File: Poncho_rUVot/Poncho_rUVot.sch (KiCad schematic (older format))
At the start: 20 parts, among them J1 Screw_Terminal_01x03, K1 G5V-1, P1 Conn_01x03, P2 Conn_01x03, P3 Conn_01x04, P4 Conn_01x03, P5 Conn_01x02, P6 Conn_01x02, P7 Conn_01x06, P8 Conn_01x04, P9 Conn_01x08, Q1 BC548, Q2 BC548

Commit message: Se elimina erro electrico en esquematico
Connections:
- net labels removed: GNDA, GNDD
- wire segments 144 -> 135
- no-connect marks 37 -> 44
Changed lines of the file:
@@
-	1    0    0    -1
-$EndComp
-$Comp
-L Poncho_rUVot-rescue:GND #PWR06
-U 1 1 57A7A207
-P 3000 3550
-F 0 "#PWR06" H 3000 3550 30  0001 C CNN
-F 1 "GND" H 3000 3480 30  0001 C CNN
-F 2 "" H 3000 3550 60  0000 C CNN
-F 3 "" H 3000 3550 60  0000 C CNN
-	1    3000 3550
 	1    0    0    -1
 $EndComp
@@
 	1    0    0    -1
 $EndComp
-$Comp
-L Poncho_rUVot-rescue:GNDD #PWR012
-U 1 1 57A7AB5F
-P 1400 6700
-F 0 "#PWR012" H 1400 6450 50  0001 C CNN
-F 1 "GNDD" H 1400 6550 50  0000 C CNN
-F 2 "" H 1400 6700 50  0000 C CNN
-F 3 "" H 1400 6700 50  0000 C CNN
-	1    1400 6700
-	1    0    0    -1
-$EndComp
-$Comp
-L Poncho_rUVot-rescue:GNDA #PWR016
-U 1 1 57A7AE2B
-P 3300 1900
-F 0 "#PWR016" H 3300 1650 50  0001 C CNN
-F 1 "GNDA" H 3300 1750 50  0000 C CNN
-F 2 "" H 3300 1900 50  0000 C CNN
-F 3 "" H 3300 1900 50  0000 C CNN
-	1    3300 1900
-	1    0    0    -1
-$EndComp
-$Comp
-L Poncho_rUVot-rescue:GNDA #PWR017
-U 1 1 57A7AE5D
-P 1350 1800
-F 0 "#PWR017" H 1350 1550 50  0001 C CNN
-F 1 "GNDA" H 1350 1650 50  0000 C CNN
-F 2 "" H 1350 1800 50  0000 C CNN
-F 3 "" H 1350 1800 50  0000 C CNN
-	1    1350 1800
-	1    0    0    -1
-$EndComp
-Wire Wire Line
-	1600 1750 1350 1750
-Wire Wire Line
-	1350 1750 1350 1800
 Wire Wire Line
 	2800 1750 2850 1750
 Wire Wire Line
-	2850 1750 2850 1850
-Wire Wire Line
 	2850 2250 2800 2250
 Wire Wire Line
 	2800 2150 2850 2150
-Connection ~ 2850 2150
 Wire Wire Line
 	2800 2050 2850 2050
-Connection ~ 2850 2050
 Wire Wire Line
 	2800 1950 2850 1950
-Connection ~ 2850 1950
 Wire Wire Line
 	2800 1850 2850 1850
-Connection ~ 2850 1850
-Wire Wire Line
-	3300 1850 3300 1900
 Wire Wire Line
 	1600 4650 1250 4650
@@
 Wire Wire Line
 	1400 4850 1400 4950
-Wire Wire Line
-	2850 2150 2850 2250
-Wire Wire Line
-	2850 2050 2850 2150
-Wire Wire Line
-	2850 1950 2850 2050
-Wire Wire Line
-	2850 1850 2850 1950
-Wire Wire Line
-	2850 1850 3300 1850
 $Comp
 L conectores-rescue:+5V-power #PWR0105
@@
 Wire Notes Line
 	750  750  750  7150
+$Comp
+L conectores-rescue:GND-power #PWR0111
+U 1 1 608EC6E9
+P 1400 6700
+F 0 "#PWR0111" H 1400 6450 50  0001 C CNN
+F 1 "GND" H 1405 6527 50  0000 C CNN
+F 2 "" H 1400 6700 50  0001 C CNN
+F 3 "" H 1400 6700 50  0001 C CNN
+	1    1400 6700
+	1    0    0    -1
+$EndComp
+$Comp
+L conectores-rescue:GND-power #PWR0112
+U 1 1 608FA01E
+P 3000 3550
+F 0 "#PWR0112" H 3000 3300 50  0001 C CNN
+F 1 "GND" H 3005 3377 50  0000 C CNN
+F 2 "" H 3000 3550 50  0001 C CNN
+F 3 "" H 3000 3550 50  0001 C CNN
+	1    3000 3550
+	1    0    0    -1
+$EndComp
+NoConn ~ 1600 1750
+NoConn ~ 2850 1750
+NoConn ~ 2850 1850
+NoConn ~ 2850 1950
+NoConn ~ 2850 2050
+NoConn ~ 2850 2150
+NoConn ~ 2850 2250
 $EndSCHEMATC

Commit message: actualizacion
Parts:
- BZ1: footprint Buzzers_Beepers:BUZZER -> Buzzer_Beeper:Buzzer_12x9.5RM7.6; symbol conectores-rescue:Buzzer-Device -> Poncho_rUVot-rescue:Buzzer-Device-conectores-rescue
- D1: footprint Diodes_THT:D_DO-35_SOD27_P2.54mm_Vertical_AnodeUp -> Diode_THT:D_DO-35_SOD27_P10.16mm_Horizontal; symbol conectores-rescue:1N4148-Diode -> Poncho_rUVot-rescue:1N4148-Diode-conectores-rescue
- D2: footprint LEDs:LED_D5.0mm -> LED_THT:LED_D5.0mm; symbol conectores-rescue:LED-Device -> Poncho_rUVot-rescue:LED-Device-conectores-rescue
- J1: symbol conectores-rescue:Screw_Terminal_01x03-Connector -> Poncho_rUVot-rescue:Screw_Terminal_01x03-Connector-conectores-rescue
- K1: footprint TerminalBlock:TerminalBlock_bornier-3_P5.08mm -> Relay_THT:Relay_SPDT_Omron_G5V-1; symbol conectores-rescue:G5V-1-Relay -> Poncho_rUVot-rescue:G5V-1-Relay-conectores-rescue
- P1, P2, P4: symbol conectores-rescue:Conn_01x03-Connector_Generic -> Poncho_rUVot-rescue:Conn_01x03-Connector_Generic-conectores-rescue
- P3, P8: symbol conectores-rescue:Conn_01x04-Connector_Generic -> Poncho_rUVot-rescue:Conn_01x04-Connector_Generic-conectores-rescue
- P5, P6: symbol conectores-rescue:Conn_01x02-Connector_Generic -> Poncho_rUVot-rescue:Conn_01x02-Connector_Generic-conectores-rescue
- P7: symbol conectores-rescue:Conn_01x06-Connector_Generic -> Poncho_rUVot-rescue:Conn_01x06-Connector_Generic-conectores-rescue
- P9: symbol conectores-rescue:Conn_01x08-Connector_Generic -> Poncho_rUVot-rescue:Conn_01x08-Connector_Generic-conectores-rescue
- Q1, Q2: symbol conectores-rescue:BC548-Transistor_BJT -> Poncho_rUVot-rescue:BC548-Transistor_BJT-conectores-rescue
- R1, R2, R4: symbol conectores-rescue:R-Device -> Poncho_rUVot-rescue:R-Device-conectores-rescue
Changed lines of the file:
@@
 	1400 4850 1400 4950
 $Comp
-L conectores-rescue:+5V-power #PWR0105
+L Poncho_rUVot-rescue:+5V-power-conectores-rescue #PWR0105
 U 1 1 6045382A
 P 5900 1500
@@
 $EndComp
 $Comp
-L conectores-rescue:GND-power #PWR0106
+L Poncho_rUVot-rescue:GND-power-conectores-rescue #PWR0106
 U 1 1 60453830
 P 5900 1600
@@
 $EndComp
 $Comp
-L conectores-rescue:Conn_01x04-Connector_Generic P3
+L Poncho_rUVot-rescue:Conn_01x04-Connector_Generic-conectores-rescue P3
 U 1 1 60453DD7
 P 6650 1600
@@
 $EndComp
 $Comp
-L conectores-rescue:GND-power #PWR0108
+L Poncho_rUVot-rescue:GND-power-conectores-rescue #PWR0108
 U 1 1 6045EF95
 P 7250 2200
@@
 $EndComp
 $Comp
-L conectores-rescue:Conn_01x02-Connector_Generic P6
+L Poncho_rUVot-rescue:Conn_01x02-Connector_Generic-conectores-rescue P6
 U 1 1 6045EFA2
 P 8000 2200
@@
 $EndComp
 $Comp
-L conectores-rescue:Conn_01x03-Connector_Generic P4
+L Poncho_rUVot-rescue:Conn_01x03-Connector_Generic-conectores-rescue P4
 U 1 1 60461281
 P 6650 2450
@@
 $EndComp
 $Comp
-L conectores-rescue:+5V-power #PWR0109
+L Poncho_rUVot-rescue:+5V-power-conectores-rescue #PWR0109
 U 1 1 6046128B
 P 5900 2350
@@
 $EndComp
 $Comp
-L conectores-rescue:GND-power #PWR0110
+L Poncho_rUVot-rescue:GND-power-conectores-rescue #PWR0110
 U 1 1 60461295
 P 5900 2450
@@
 $EndComp
 $Comp
-L conectores-rescue:Conn_01x04-Connector_Generic P8
+L Poncho_rUVot-rescue:Conn_01x04-Connector_Generic-conectores-rescue P8
 U 1 1 60476D23
 P 10550 2900
@@
 $EndComp
 $Comp
-L conectores-rescue:Buzzer-Device BZ1
+L Poncho_rUVot-rescue:Buzzer-Device-conectores-rescue BZ1
 U 1 1 604E6A0D
 P 10350 4850
 F 0 "BZ1" H 10355 5140 50  0000 C CNN
 F 1 "Buzzer" H 10355 5049 50  0000 C CNN
-F 2 "Buzzers_Beepers:BUZZER" V 10325 4950 50  0001 C CNN
+F 2 "Buzzer_Beeper:Buzzer_12x9.5RM7.6" V 10325 4950 50  0001 C CNN
 F 3 "~" V 10325 4950 50  0001 C CNN
 	1    10350 4850
@@
 $EndComp
 $Comp
-L conectores-rescue:BC548-Transistor_BJT Q2
+L Poncho_rUVot-rescue:BC548-Transistor_BJT-conectores-rescue Q2
 U 1 1 604E7631
 P 10350 5550
@@
 $EndComp
 $Comp
-L conectores-rescue:+5V-power #PWR0113
+L Poncho_rUVot-rescue:+5V-power-conectores-rescue #PWR0113
 U 1 1 604E9C31
 P 10450 4100
@@
 	10450 4950 10450 5350
 $Comp
-L conectores-rescue:GND-power #PWR0114
+L Poncho_rUVot-rescue:GND-power-conectores-rescue #PWR0114
 U 1 1 604EC141
 P 10450 5900
@@
 $EndComp
 $Comp
-L conectores-rescue:R-Device R2
+L Poncho_rUVot-rescue:R-Device-conectores-rescue R2
 U 1 1 604EDEF3
 P 9850 5550
@@
 	9050 3750 10950 3750
 $Comp
-L conectores-rescue:+5V-power #PWR0115
+L Poncho_rUVot-rescue:+5V-power-conectores-rescue #PWR0115
 U 1 1 605294A9
 P 9450 1350
@@
 $EndComp
 $Comp
-L conectores-rescue:GND-power #PWR0116
+L Poncho_rUVot-rescue:GND-power-conectores-rescue #PWR0116
 U 1 1 60529813
 P 9450 1450
@@
 $EndComp
 $Comp
-L conectores-rescue:Conn_01x06-Connector_Generic P7
+L Poncho_rUVot-rescue:Conn_01x06-Connector_Generic-conectores-rescue P7
 U 1 1 6052981E
 P 10550 1450
@@
 Conector Módulo Bluetooth
 $Comp
-L conectores-rescue:+5V-power #PWR0117
+L Poncho_rUVot-rescue:+5V-power-conectores-rescue #PWR0117
 U 1 1 60530A10
 P 7650 4100
@@
 $EndComp
 $Comp
-L conectores-rescue:R-Device R1
+L Poncho_rUVot-rescue:R-Device-conectores-rescue R1
 U 1 1 60530A27
 P 7050 5550
@@
 Connection ~ 8150 4400
 $Comp
-L conectores-rescue:G5V-1-Relay K1
+L Poncho_rUVot-rescue:G5V-1-Relay-conectores-rescue K1
 U 1 1 60534F55
 P 7850 4700
 F 0 "K1" H 8280 4700 50  0000 L CNN
 F 1 "G5V-1" H 8280 4655 50  0001 L CNN
-F 2 "TerminalBlock:TerminalBlock_bornier-3_P5.08mm" H 8280 4655 50  0001 L CNN
+F 2 "Relay_THT:Relay_SPDT_Omron_G5V-1" H 8280 4655 50  0001 L CNN
 F 3 "http://omronfs.omron.com/en_US/ecb/products/pdf/en-g5v_1.pdf" H 7850 4700 50  0001 C CNN
 	1    7850 4700
@@
 Conector Driver MOTOR
 $Comp
-L conectores-rescue:Screw_Terminal_01x03-Connector J1
+L Poncho_rUVot-rescue:Screw_Terminal_01x03-Connector-conectores-rescue J1
 U 1 1 606412BA
 P 8600 4150
@@
 	8400 4050 8450 4050
 $Comp
-L conectores-rescue:1N4148-Diode D1
+L Poncho_rUVot-rescue:1N4148-Diode-conectores-rescue D1
 U 1 1 60659DD3
 P 7050 4700
 F 0 "D1" V 7004 4780 50  0000 L CNN
 F 1 "1N4148" V 7095 4780 50  0000 L CNN
-F 2 "Diodes_THT:D_DO-35_SOD27_P2.54mm_Vertical_AnodeUp" H 7050 4525 50  0001 C CNN
+F 2 "Diode_THT:D_DO-35_SOD27_P10.16mm_Horizontal" H 7050 4525 50  0001 C CNN
 F 3 "https://assets.nexperia.com/documents/data-sheet/1N4148_1N4448.pdf" H 7050 4700 50  0001 C CNN
 	1    7050 4700
@@
 	7650 5150 7650 5350
 $Comp
-L conectores-rescue:R-Device R4
+L Poncho_rUVot-rescue:R-Device-conectores-rescue R4
 U 1 1 6069C7E8
 P 6700 4500
@@
 $EndComp
 $Comp
-L conectores-rescue:LED-Device D2
+L Poncho_rUVot-rescue:LED-Device-conectores-rescue D2
 U 1 1 6069CC76
 P 6700 4800
 F 0 "D2" V 6739 4682 50  0000 R CNN
 F 1 "LED" V 6648 4682 50  0000 R CNN
-F 2 "LEDs:LED_D5.0mm" H 6700 4800 50  0001 C CNN
+F 2 "LED_THT:LED_D5.0mm" H 6700 4800 50  0001 C CNN
 F 3 "~" H 6700 4800 50  0001 C CNN
 	1    6700 4800
@@
 Conector I2C Acelerómetro\n
 $Comp
-L conectores-rescue:Conn_01x08-Connector_Generic P9
+L Poncho_rUVot-rescue:Conn_01x08-Connector_Generic-conectores-rescue P9
 U 1 1 606C4AD7
 P 5350 4600
@@
 $EndComp
 $Comp
-L conectores-rescue:+5V-power #PWR0121
+L Poncho_rUVot-rescue:+5V-power-conectores-rescue #PWR0121
 U 1 1 606CBFD5
 P 4450 4300
@@
 $EndComp
 $Comp
-L conectores-rescue:GND-power #PWR0122
+L Poncho_rUVot-rescue:GND-power-conectores-rescue #PWR0122
 U 1 1 606CC4AB
 P 4450 4450
@@
 	6050 3750 6050 5200
 $Comp
-L conectores-rescue:GND-power #PWR0123
+L Poncho_rUVot-rescue:GND-power-conectores-rescue #PWR0123
 U 1 1 605D65B8
 P 7650 5900
@@
 $EndComp
 $Comp
-L conectores-rescue:BC548-Transistor_BJT Q1
+L Poncho_rUVot-rescue:BC548-Transistor_BJT-conectores-rescue Q1
 U 1 1 60530A06
 P 7550 5550
@@
 	7700 2300 7800 2300
 $Comp
-L conectores-rescue:GND-power #PWR0107
+L Poncho_rUVot-rescue:GND-power-conectores-rescue #PWR0107
 U 1 1 60729492
 P 7250 1600
@@
 $EndComp
 $Comp
-L conectores-rescue:Conn_01x02-Connector_Generic P5
+L Poncho_rUVot-rescue:Conn_01x02-Connector_Generic-conectores-rescue P5
 U 1 1 60729499
 P 8000 1600
@@
 GPIO6
 $Comp
-L conectores-rescue:Conn_01x03-Connector_Generic P1
+L Poncho_rUVot-rescue:Conn_01x03-Connector_Generic-conectores-rescue P1
 U 1 1 60731B65
 P 5200 1600
@@
 $EndComp
 $Comp
-L conectores-rescue:+5V-power #PWR0101
+L Poncho_rUVot-rescue:+5V-power-conectores-rescue #PWR0101
 U 1 1 60731B6B
 P 4450 1500
@@
 $EndComp
 $Comp
-L conectores-rescue:GND-power #PWR0102
+L Poncho_rUVot-rescue:GND-power-conectores-rescue #PWR0102
 U 1 1 60731B71
 P 4450 1600
@@
 	4900 1700 5000 1700
 $Comp
-L conectores-rescue:Conn_01x03-Connector_Generic P2
+L Poncho_rUVot-rescue:Conn_01x03-Connector_Generic-conectores-rescue P2
 U 1 1 6074F498
 P 5200 2450
@@
 $EndComp
 $Comp
-L conectores-rescue:+5V-power #PWR0103
+L Poncho_rUVot-rescue:+5V-power-conectores-rescue #PWR0103
 U 1 1 6074F49E
 P 4450 2350
@@
 $EndComp
 $Comp
-L conectores-rescue:GND-power #PWR0104
+L Poncho_rUVot-rescue:GND-power-conectores-rescue #PWR0104
 U 1 1 6074F4A4
 P 4450 2450
@@
 	750  750  750  7150
 $Comp
-L conectores-rescue:GND-power #PWR0111
+L Poncho_rUVot-rescue:GND-power-conectores-rescue #PWR0111
 U 1 1 608EC6E9
 P 1400 6700
@@
 $EndComp
 $Comp
-L conectores-rescue:GND-power #PWR0112
+L Poncho_rUVot-rescue:GND-power-conectores-rescue #PWR0112
 U 1 1 608FA01E
 P 3000 3550

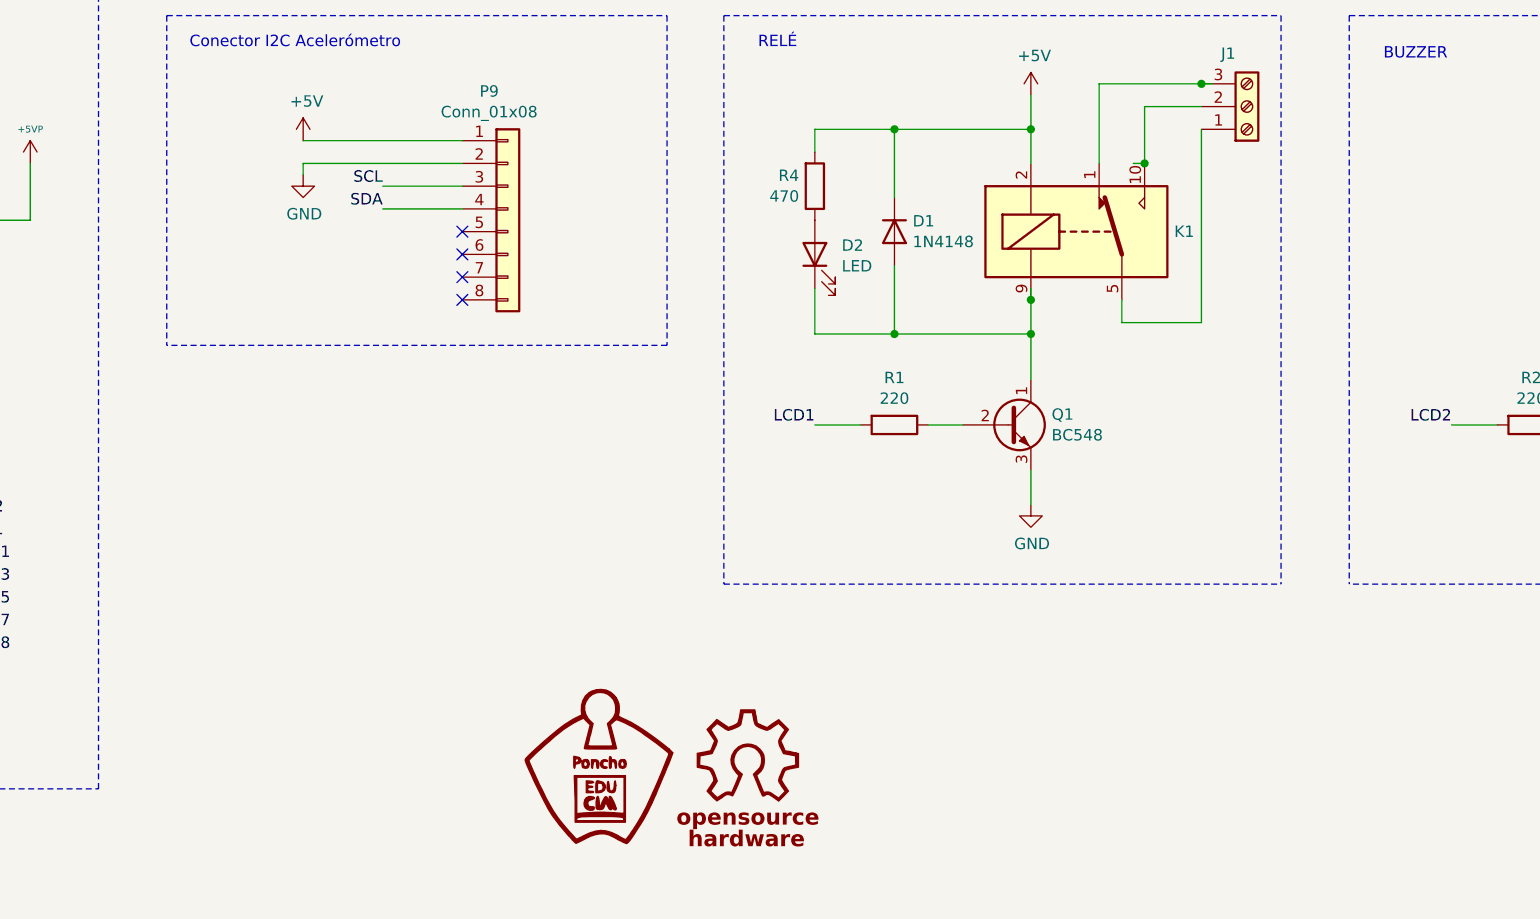
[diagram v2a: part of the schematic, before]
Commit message: Se hacen correciones indicadas en el esquematico
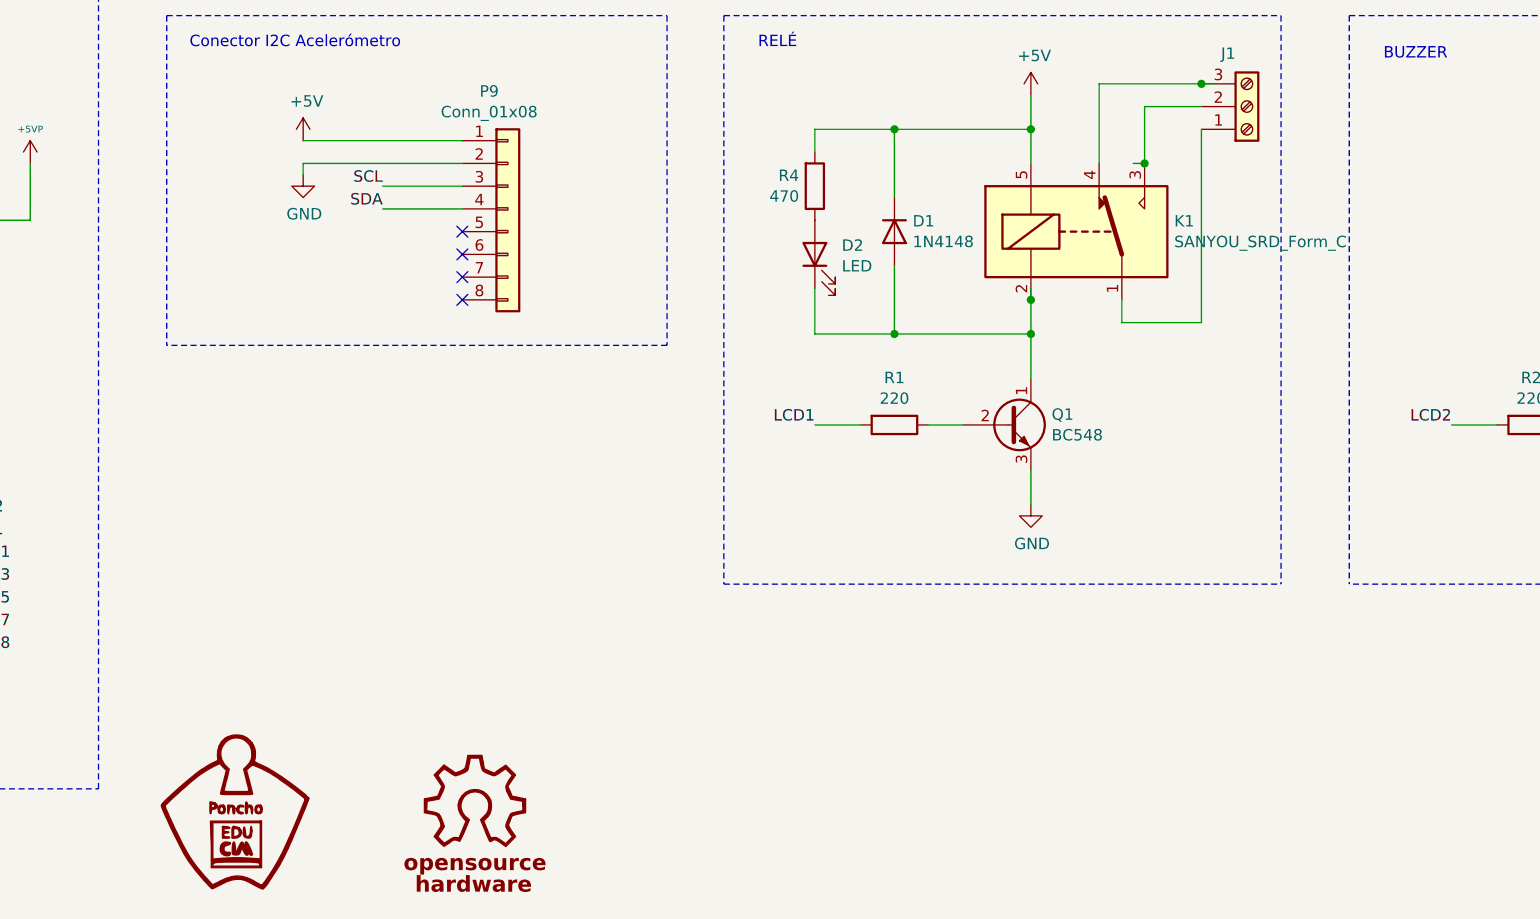
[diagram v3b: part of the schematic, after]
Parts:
- removed K1: G5V-1, Relay_THT:Relay_SPDT_Omron_G5V-1, symbol Poncho_rUVot-rescue:G5V-1-Relay-conectores-rescue
- added K1: SANYOU_SRD_Form_C, Relay_THT:Relay_SPDT_SANYOU_SRD_Series_Form_C, symbol Relay:SANYOU_SRD_Form_C
- J1: footprint TerminalBlock:TerminalBlock_bornier-3_P5.08mm -> TerminalBlock_Phoenix:TerminalBlock_Phoenix_MKDS-1,5-3-5.08_1x03_P5.08mm_Horizontal
- P1, P2, P4: footprint Connector_PinHeader_1.00mm:PinHeader_1x03_P1.00mm_Horizontal -> Connector_PinHeader_2.54mm:PinHeader_1x03_P2.54mm_Horizontal
- P3, P8: footprint Connector_PinHeader_1.00mm:PinHeader_1x04_P1.00mm_Horizontal -> Connector_PinHeader_2.54mm:PinHeader_1x04_P2.54mm_Horizontal
- P5, P6: footprint Connector_PinHeader_1.00mm:PinHeader_1x02_P1.00mm_Horizontal -> Connector_PinHeader_2.54mm:PinHeader_1x02_P2.54mm_Horizontal
- P7: footprint Connector_PinSocket_1.00mm:PinSocket_1x06_P1.00mm_Vertical -> Connector_PinSocket_2.54mm:PinSocket_1x06_P2.54mm_Vertical
- P9: footprint Connector_PinSocket_1.00mm:PinSocket_1x08_P1.00mm_Vertical -> Connector_PinSocket_2.54mm:PinSocket_1x08_P2.54mm_Vertical
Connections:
- net +5V: now also K1.5
- net at D1.2 (A), D2.1 (K), Q1.1 (C): now also K1.2
- net at J1.3 (Pin_3): now also K1.4
- net at J1.2 (Pin_2): now also K1.3
- net at J1.1 (Pin_1): now also K1.1
